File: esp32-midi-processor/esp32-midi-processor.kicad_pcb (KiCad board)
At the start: 2 copper layers, 50 parts, among them J1 Midi IN 1, J10 USB Shield right, J11 Spare, J12 Display, J2 Midi IN 2, J3 Midi OUT 1, J4 Midi OUT 2, J5 ESP32 right, J6 ESP32 left, J7 Input Voltage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

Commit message: new pcb revision
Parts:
- moved SW4 191.0 mm to (203.2, 106.6), turned to 90 degrees
- moved SW3 178.9 mm to (186.7, 106.6), turned to 90 degrees
- moved R15 176.3 mm to (209.8, 89.3), turned to 90 degrees
- moved R14 162.9 mm to (194.1, 89.3), turned to 90 degrees
- moved J7 161.3 mm to (174.0, 33.5)
- moved C6 160.9 mm to (211.9, 48.1), turned to -90 degrees
- moved SW2 160.7 mm to (161.3, 106.6), turned to 90 degrees
- moved D6 160.5 mm to (205.7, 48.3)
- moved SW1 155.3 mm to (147.3, 106.7), turned to 90 degrees
- moved D5 143.7 mm to (189.2, 48.3)
- moved R13 142.2 mm to (168.3, 89.3), turned to 90 degrees
- moved C5 141.4 mm to (195.4, 48.4), turned to -90 degrees
- moved R12 135.3 mm to (153.9, 89.5), turned to 90 degrees
- moved R16 132.9 mm to (205.7, 64.8)
- moved D7 132.3 mm to (176.5, 85.1)
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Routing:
- net (no net): vias 0 -> 4

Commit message: Next PCB version
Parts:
- moved J11 143.4 mm to (23.1, 57.4)
- moved J9 130.7 mm to (112.5, 49.8), turned to 180 degrees
- moved JP1 130.1 mm to (121.4, 49.1), turned to 90 degrees
- moved J5 128.1 mm to (53.3, 81.5)
- moved J6 128.1 mm to (27.9, 81.5)
- moved J10 127.7 mm to (99.8, 67.6), turned to 180 degrees
- moved R1 121.7 mm to (36.0, 45.7)
- moved R4 121.5 mm to (52.5, 45.7)
- moved R10 118.2 mm to (84.4, 47.0)
- moved R9 117.9 mm to (91.4, 45.7)
- moved R8 117.7 mm to (68.4, 46.7)
- moved C6 116.7 mm to (95.3, 45.7), turned to 0 degrees
- moved J4 116.0 mm to (90.2, 35.6)
- moved J1 116.0 mm to (31.8, 35.4)
- moved J2 116.0 mm to (48.1, 35.4)
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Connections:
- D3 pad 1: +5V -> GND
- D3 pad 2: Net-(D3-DOUT) -> LED_DATA
- D3 pad 3: GND -> +5V
- D3 pad 4: LED_DATA -> Net-(D3-DOUT)
- D4 pad 1: +5V -> GND
- D4 pad 2: Net-(D4-DOUT) -> Net-(D3-DOUT)
- D4 pad 3: GND -> +5V
- D4 pad 4: Net-(D3-DOUT) -> Net-(D4-DOUT)
- D5 pad 1: +5V -> GND
- D5 pad 2: Net-(D5-DOUT) -> Net-(D4-DOUT)
- D5 pad 3: GND -> +5V
- D5 pad 4: Net-(D4-DOUT) -> Net-(D5-DOUT)
- D6 pad 1: +5V -> GND
- D6 pad 2: Net-(D6-DOUT) -> Net-(D5-DOUT)
- D6 pad 3: GND -> +5V
- D6 pad 4: Net-(D5-DOUT) -> Net-(D6-DOUT)
- D7 pad 1: +5V -> GND
- D7 pad 2: unconnected-(D7-DOUT-Pad2) -> Net-(D6-DOUT)
- D7 pad 3: GND -> +5V
- D7 pad 4: Net-(D6-DOUT) -> unconnected-(D7-DOUT-Pad4)
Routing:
- net Net-(J9-Pin_1): vias 0 -> 1
- net (no net): vias 4 -> 3
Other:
- board outline added: 108 x 100 mm
- board text added: "5V USB Power Cut trace on board when used"
- board text added: "Andy Fischer info@Andyland.info"
- board text added: "Rev xxx"
- board text added: "Spare"
- board text added: "esp32 Midi Processor"

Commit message: finetune PCB layout
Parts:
- moved J11 45.5 mm to (22.1, 102.9)
- moved C7 8.68 mm to (119.1, 86.4), turned to 90 degrees
- moved JP1 3.64 mm to (120.7, 52.7)
- moved R16 2.32 mm to (106.6, 72.6)
- moved SW5 1.98 mm to (94.6, 78.8)
- moved D7 0.75 mm to (117.3, 80.8), turned to 90 degrees
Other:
- board text added: "Display"
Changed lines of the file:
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@@
 	(footprint "Rotary_Encoder:RotaryEncoder_Alps_EC11E-Switch_Vertical_H20mm"
 		(layer "F.Cu")
-		(at 93.08 77.51)
+		(at 94.604 78.78)
 		(descr "Alps rotary encoder, EC12E... with switch, vertical shaft, http://www.alps.com/prod/info/E/HTML/Encoder/Incremental/EC11/EC11E15204A3.html")
 		(tags "rotary encoder")
@@
 	(footprint "Capacitor_SMD:C_0603_1608Metric"
 		(layer "F.Cu")
-		(at 37.926 50.812 -90)
+		(at 37.926001 50.811999 -90)
 		(descr "Capacitor SMD 0603 (1608 Metric), square (rectangular) end terminal, IPC_7351 nominal, (Body size source: IPC-SM-782 page 76, https://www.pcb-3d.com/wordpress/wp-content/uploads/ipc-sm-782a_amendment_1_and_2.pdf), generated with kicad-footprint-generator")
 		(tags "capacitor")
@@
 	(footprint "Resistor_SMD:R_0603_1608Metric"
 		(layer "F.Cu")
-		(at 105.981 70.358)
+		(at 106.564 72.604)
 		(descr "Resistor SMD 0603 (1608 Metric), square (rectangular) end terminal, IPC_7351 nominal, (Body size source: IPC-SM-782 page 72, https://www.pcb-3d.com/wordpress/wp-content/uploads/ipc-sm-782a_amendment_1_and_2.pdf), generated with kicad-footprint-generator")
 		(tags "resistor")
 		(property "Reference" "R16"
-			(at 0 -1.43 0)
+			(at -2.985 0 0)
 			(layer "F.SilkS")
 			(effects
@@
 		)
 		(property "Value" "10k"
-			(at 0 1.43 0)
+			(at 2.857 0 0)
 			(layer "F.Fab")
 			(effects
@@
 	(footprint "LED_SMD:LED_WS2812B_PLCC4_5.0x5.0mm_P3.2mm"
 		(layer "F.Cu")
-		(at 31.75 50.8)
+		(at 31.750001 50.799999)
 		(descr "5.0mm x 5.0mm Addressable RGB LED NeoPixel, https://cdn-shop.adafruit.com/datasheets/WS2812B.pdf")
 		(tags "LED RGB NeoPixel PLCC-4 5050")
 		(property "Reference" "D3"
-			(at 0 -3.5 0)
+			(at 0 -3.5 360)
 			(layer "F.SilkS")
 			(effects
@@
 		)
 		(property "Value" "WS2812B"
-			(at 0 4 0)
+			(at 0 4 360)
 			(layer "F.Fab")
 			(effects
@@
 		)
 		(fp_text user "1"
-			(at -4.15 -1.6 0)
+			(at -4.15 -1.6 360)
 			(layer "F.SilkS")
 			(effects
@@
 		)
 		(fp_text user "${REFERENCE}"
-			(at 0 0 0)
+			(at 0 0 360)
 			(layer "F.Fab")
 			(effects
@@
 	(footprint "Capacitor_SMD:C_0603_1608Metric"
 		(layer "F.Cu")
-		(at 111.747 81.788)
+		(at 119.126 86.36 90)
 		(descr "Capacitor SMD 0603 (1608 Metric), square (rectangular) end terminal, IPC_7351 nominal, (Body size source: IPC-SM-782 page 76, https://www.pcb-3d.com/wordpress/wp-content/uploads/ipc-sm-782a_amendment_1_and_2.pdf), generated with kicad-footprint-generator")
 		(tags "capacitor")
 		(property "Reference" "C7"
-			(at 0 -1.43 360)
+			(at 0 -1.43 90)
 			(layer "F.SilkS")
 			(effects
@@
 		)
 		(property "Value" "0.1µ"
-			(at 0 1.43 360)
+			(at 0 1.43 90)
 			(layer "F.Fab")
 			(effects
@@
 		)
 		(property "Footprint" "Capacitor_SMD:C_0603_1608Metric"
-			(at 0 0 0)
+			(at 0 0 90)
 			(unlocked yes)
 			(layer "F.Fab")
@@
 		)
 		(property "Datasheet" ""
-			(at 0 0 0)
+			(at 0 0 90)
 			(unlocked yes)
 			(layer "F.Fab")
@@
 		)
 		(property "Description" ""
-			(at 0 0 0)
+			(at 0 0 90)
 			(unlocked yes)
 			(layer "F.Fab")
@@
 		)
 		(fp_line
-			(start -1.48 -0.73)
-			(end 1.48 -0.73)
+			(start 1.48 -0.73)
+			(end 1.48 0.73)
 			(stroke
 				(width 0.05)
@@
 		)
 		(fp_line
-			(start -1.48 0.73)
-			(end -1.48 -0.73)
+			(start -1.48 -0.73)
+			(end 1.48 -0.73)
 			(stroke
 				(width 0.05)
@@
 		)
 		(fp_line
-			(start 1.48 -0.73)
-			(end 1.48 0.73)
+			(start 1.48 0.73)
+			(end -1.48 0.73)
 			(stroke
 				(width 0.05)
@@
 		)
 		(fp_line
-			(start 1.48 0.73)
-			(end -1.48 0.73)
+			(start -1.48 0.73)
+			(end -1.48 -0.73)
 			(stroke
 				(width 0.05)
@@
 		)
 		(fp_line
-			(start -0.8 -0.4)
-			(end 0.8 -0.4)
+			(start 0.8 -0.4)
+			(end 0.8 0.4)
 			(stroke
 				(width 0.1)
@@
 		)
 		(fp_line
-			(start -0.8 0.4)
-			(end -0.8 -0.4)
+			(start -0.8 -0.4)
+			(end 0.8 -0.4)
 			(stroke
 				(width 0.1)
@@
 		)
 		(fp_line
-			(start 0.8 -0.4)
-			(end 0.8 0.4)
+			(start 0.8 0.4)
+			(end -0.8 0.4)
 			(stroke
 				(width 0.1)
@@
 		)
 		(fp_line
-			(start 0.8 0.4)
-			(end -0.8 0.4)
+			(start -0.8 0.4)
+			(end -0.8 -0.4)
 			(stroke
 				(width 0.1)
@@
 		)
 		(fp_text user "${REFERENCE}"
-			(at 0 0 360)
+			(at 0 0 90)
 			(layer "F.Fab")
 			(effects
@@
 		)
 		(pad "1" smd roundrect
-			(at -0.775 0)
+			(at -0.775 0 90)
 			(size 0.9 0.95)
 			(layers "F.Cu" "F.Paste" "F.Mask")
@@
 		)
 		(pad "2" smd roundrect
-			(at 0.775 0)
+			(at 0.775 0 90)
 			(size 0.9 0.95)
 			(layers "F.Cu" "F.Paste" "F.Mask")
@@
 	(footprint "Jumper:SolderJumper-2_P1.3mm_Open_RoundedPad1.0x1.5mm"
 		(layer "F.Cu")
-		(at 121.412 49.134 90)
+		(at 120.65 52.69 90)
 		(descr "SMD Solder Jumper, 1x1.5mm, rounded Pads, 0.3mm gap, open")
 		(tags "solder jumper open")
 		(property "Reference" "JP1"
-			(at 0 -1.8 90)
+			(at 3.16 0 90)
 			(layer "F.SilkS")
 			(effects
@@
 	(footprint "Connector_PinHeader_2.54mm:PinHeader_1x05_P2.54mm_Vertical"
 		(layer "F.Cu")
-		(at 23.114 57.404 180)
+		(at 22.098 102.87 180)
 		(descr "Through hole straight pin header, 1x05, 2.54mm pitch, single row")
 		(tags "Through hole pin header THT 1x05 2.54mm single row")
@@
 	(footprint "LED_SMD:LED_WS2812B_PLCC4_5.0x5.0mm_P3.2mm"
 		(layer "F.Cu")
-		(at 117.348 80.01)
+		(at 117.348 80.759 90)
 		(descr "5.0mm x 5.0mm Addressable RGB LED NeoPixel, https://cdn-shop.adafruit.com/datasheets/WS2812B.pdf")
 		(tags "LED RGB NeoPixel PLCC-4 5050")
 		(property "Reference" "D7"
-			(at 0 -3.5 0)
+			(at 0 -3.5 90)
 			(layer "F.SilkS")
 			(effects
@@
 		)
 		(property "Value" "WS2812B"
-			(at 0 4 0)
+			(at 0 4 90)
 			(layer "F.Fab")
 			(effects
@@
 		)
 		(property "Footprint" "LED_SMD:LED_WS2812B_PLCC4_5.0x5.0mm_P3.2mm"
-			(at 0 0 0)
+			(at 0 0 90)
 			(unlocked yes)
 			(layer "F.Fab")
@@
 		)
 		(property "Datasheet" "https://cdn-shop.adafruit.com/datasheets/WS2812B.pdf"
-			(at 0 0 0)
+			(at 0 0 90)
 			(unlocked yes)
 			(layer "F.Fab")
@@
 		)
 		(property "Description" "RGB LED with integrated controller"
-			(at 0 0 0)
+			(at 0 0 90)
 			(unlocked yes)
 			(layer "F.Fab")
@@
 		(fp_line
 			(start -3.5 -2.75)
-			(end -3.5 2.75)
+			(end 3.5 -2.75)
 			(stroke
 				(width 0.12)
-				(type default)
+				(type solid)
 			)
 			(layer "F.SilkS")
@@
 		(fp_line
 			(start -3.5 -2.75)
-			(end 3.5 -2.75)
+			(end -3.5 2.75)
 			(stroke
 				(width 0.12)
-				(type solid)
+				(type default)
 			)
 			(layer "F.SilkS")
 		)
 		(fp_line
-			(start -3.5 2.75)
-			(end 3.05 2.75)
+			(start 2.7 0.9)
+			(end 2.7 -0.9)
 			(stroke
 				(width 0.12)
-				(type solid)
+				(type default)
 			)
 			(layer "F.SilkS")
@@
 		)
 		(fp_line
-			(start 2.7 0.9)
-			(end 2.7 -0.9)
+			(start 3.5 2.3)
+			(end 3.5 -2.75)
 			(stroke
 				(width 0.12)
@@
 		)
 		(fp_line
-			(start 3.5 2.3)
-			(end 3.5 -2.75)
+			(start -3.5 2.75)
+			(end 3.05 2.75)
 			(stroke
 				(width 0.12)
-				(type default)
+				(type solid)
 			)
 			(layer "F.SilkS")
 		)
 		(fp_line
-			(start -3.45 -2.75)
-			(end -3.45 2.75)
+			(start 3.45 -2.75)
+			(end -3.45 -2.75)
 			(stroke
 				(width 0.05)
@@
 		)
 		(fp_line
-			(start -3.45 2.75)
-			(end 3.45 2.75)
+			(start -3.45 -2.75)
+			(end -3.45 2.75)
 			(stroke
 				(width 0.05)
@@
 		)
 		(fp_line
-			(start 3.45 -2.75)
-			(end -3.45 -2.75)
+			(start 3.45 2.75)
+			(end 3.45 -2.75)
 			(stroke
 				(width 0.05)
@@
 		)
 		(fp_line
-			(start 3.45 2.75)
-			(end 3.45 -2.75)
+			(start -3.45 2.75)
+			(end 3.45 2.75)
 			(stroke
 				(width 0.05)
@@
 		)
 		(fp_line
-			(start -2.5 -2.5)
-			(end -2.5 2.5)
+			(start 2.5 -2.5)
+			(end -2.5 -2.5)
 			(stroke
 				(width 0.1)
@@
 		)
 		(fp_line
-			(start -2.5 2.5)
-			(end 2.5 2.5)
+			(start -2.5 -2.5)
+			(end -2.5 2.5)
 			(stroke
 				(width 0.1)
@@
 		)
 		(fp_line
-			(start 2.5 -2.5)
-			(end -2.5 -2.5)
+			(start 2.5 1.5)
+			(end 1.5 2.5)
 			(stroke
 				(width 0.1)
@@
 		)
 		(fp_line
-			(start 2.5 1.5)
-			(end 1.5 2.5)
+			(start 2.5 2.5)
+			(end 2.5 -2.5)
 			(stroke
 				(width 0.1)
@@
 		)
 		(fp_line
-			(start 2.5 2.5)
-			(end 2.5 -2.5)
+			(start -2.5 2.5)
+			(end 2.5 2.5)
 			(stroke
 				(width 0.1)
@@
 		)
 		(fp_text user "1"
-			(at -4.15 -1.6 0)
+			(at -4.15 -1.6 90)
 			(layer "F.SilkS")
 			(effects
@@
 		)
 		(fp_text user "${REFERENCE}"
-			(at 0 0 0)
+			(at 0 0 90)
 			(layer "F.Fab")
 			(effects
@@
 		)
 		(pad "1" smd roundrect
-			(at 2.45 1.65)
+			(at 2.45 1.65 90)
 			(size 1.5 0.9)
 			(layers "F.Cu" "F.Paste" "F.Mask")
@@
 		)
 		(pad "2" smd roundrect
-			(at 2.45 -1.65)
+			(at 2.45 -1.65 90)
 			(size 1.5 0.9)
 			(layers "F.Cu" "F.Paste" "F.Mask")
@@
 		)
 		(pad "3" smd roundrect
-			(at -2.45 -1.65)
+			(at -2.45 -1.65 90)
 			(size 1.5 0.9)
 			(layers "F.Cu" "F.Paste" "F.Mask")
@@
 		)
 		(pad "4" smd roundrect
-			(at -2.45 1.65)
+			(at -2.45 1.65 90)
 			(size 1.5 0.9)
 			(layers "F.Cu" "F.Paste" "F.Mask")
@@
 	)
 	(gr_text "Spare"
-		(at 19.304 48.006 -90)
+		(at 18.288 94.488 -90)
 		(layer "F.Cu")
 		(effects
@@
 		)
 	)
+	(gr_text "Display"
+		(at 72.39 68.58 0)
+		(layer "F.Cu")
+		(effects
+			(font
+				(size 1.5 1.5)
+				(thickness 0.3)
+				(bold yes)
+			)
+			(justify left bottom)
+		)
+	)
 	(gr_text "5V USB Power\nCut trace on board when used"
 		(at 123.952 72.644 90)
@@
 	)
 	(group ""
-		(members "1eb45983-e13a-4e24-a8de-6d34aea4c447" "8bb42a2d-e008-408c-bc52-eb8c33ba9f26"
-			"a2db069c-19e1-400f-bdca-d7b96c9209ce" "db5abf1f-b9d4-423e-8b6a-421774b6952d"
-		)
+		(members "0c6cbc20-25a2-419d-a57b-d6d3897a2436" "cfc32b96-ced7-4591-b225-65d6a804a9ef")
 	)
 	(group ""
-		(members "0c6cbc20-25a2-419d-a57b-d6d3897a2436" "cfc32b96-ced7-4591-b225-65d6a804a9ef")
+		(members "9f0a9885-ed78-4520-a495-1e692e11a0d3" "b498d34a-d34e-4cfa-962d-e628cba90ec7")
+	)
+	(group ""
+		(members "01be0578-2009-43a0-a3ef-1d359ff7b4c1" "449e378e-0ef0-4dff-98c3-e434a1c2ca9a")
 	)
 	(group ""

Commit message: finetune PCB layout
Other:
- board text added: "Midi IN 1"
- board text added: "Midi IN 2"
- board text added: "Midi OUT 1"
- board text added: "Midi OUT 2"
- board text added: "esp32"
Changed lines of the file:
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@@
+		)
+	)
+	(gr_text "Midi IN 1"
+		(at 25.908 44.45 90)
+		(layer "F.Cu")
+		(effects
+			(font
+				(size 1.5 1.5)
+				(thickness 0.3)
+				(bold yes)
+			)
+			(justify left bottom)
+		)
+	)
+	(gr_text "Midi IN 2"
+		(at 42.418 44.45 90)
+		(layer "F.Cu")
+		(effects
+			(font
+				(size 1.5 1.5)
+				(thickness 0.3)
+				(bold yes)
+			)
+			(justify left bottom)
+		)
+	)
+	(gr_text "esp32"
+		(at 36.068 98.298 0)
+		(layer "F.Cu")
+		(effects
+			(font
+				(size 1.5 1.5)
+				(thickness 0.3)
+				(bold yes)
+			)
+			(justify left bottom)
 		)
 	)
@@
 		)
 	)
+	(gr_text "Midi OUT 1"
+		(at 81.28 44.958 90)
+		(layer "F.Cu")
+		(effects
+			(font
+				(size 1.5 1.5)
+				(thickness 0.3)
+				(bold yes)
+			)
+			(justify left bottom)
+		)
+	)
 	(gr_text "Display"
 		(at 72.39 68.58 0)
 		(layer "F.Cu")
 		(effects
+			(font
+				(size 1.5 1.5)
+				(thickness 0.3)
+				(bold yes)
+			)
+			(justify left bottom)
+		)
+	)
+	(gr_text "Midi OUT 2"
+		(at 97.79 44.958 90)
+		(layer "F.Cu")
+		(effects

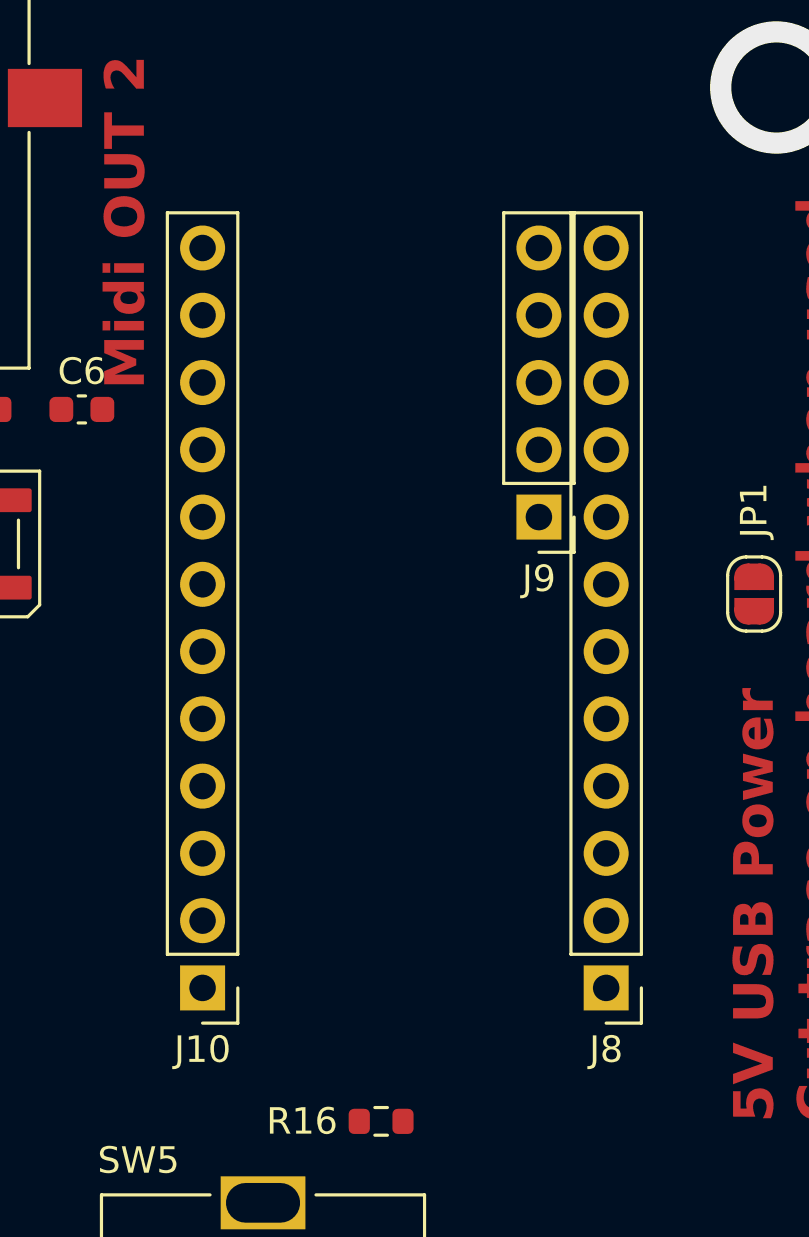
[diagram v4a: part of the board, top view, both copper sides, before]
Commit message: fix usb shield's orientation
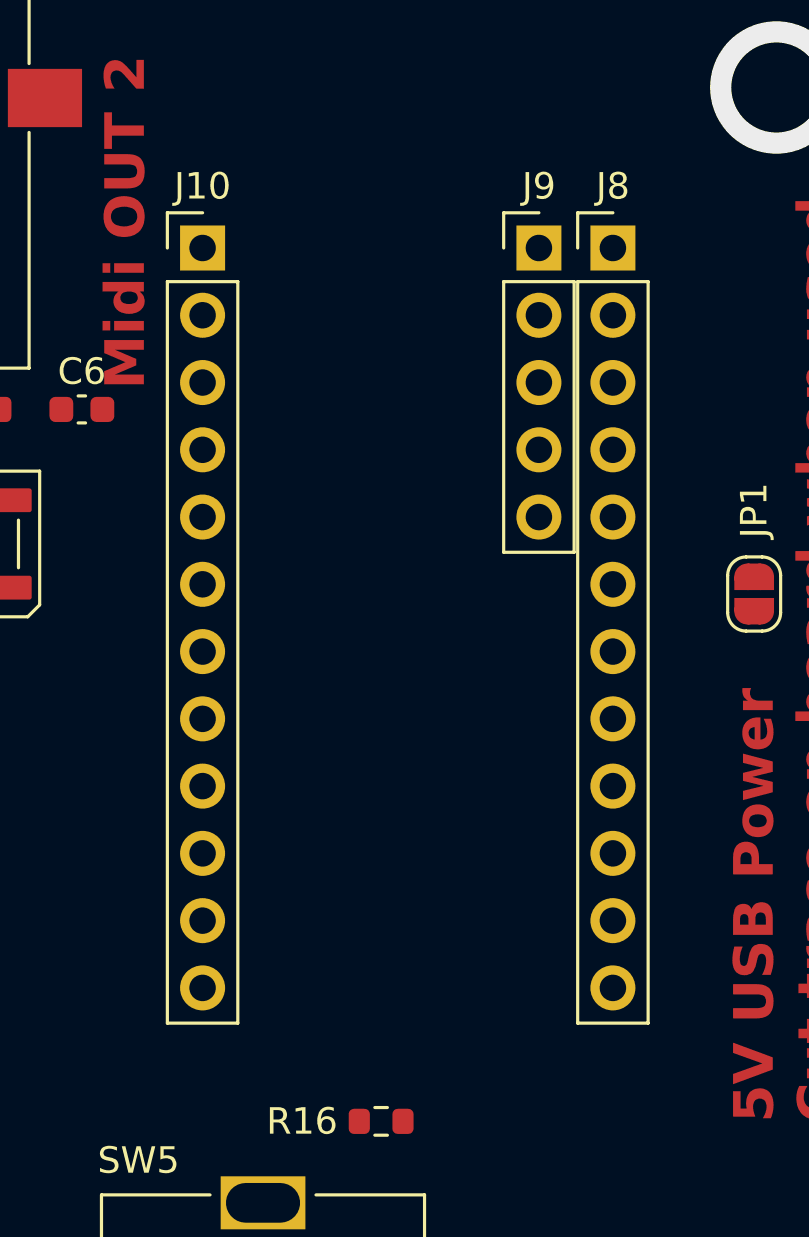
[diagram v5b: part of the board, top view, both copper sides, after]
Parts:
- moved J8 27.9 mm to (115.3, 39.6), turned to 0 degrees
- moved J10 27.9 mm to (99.8, 39.6), turned to 0 degrees
- moved J9 10.2 mm to (112.5, 39.6), turned to 0 degrees
